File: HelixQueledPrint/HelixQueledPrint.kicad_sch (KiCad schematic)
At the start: 48 parts, among them J1 USB_C_Receptacle_USB2.0_16P, J101 Conn_Coaxial, SW1 SW_SPST, SW2 SW_SPST, U101 ESP32-C6FHx, U102 BGS12WN6E6327, Y1 40MHz

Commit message: added some stuffs
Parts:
- added R17: 0R, Resistor_SMD:R_0402_1005Metric, symbol Device:R
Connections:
- net at R101.1, R102.2, U102.6 (CTRL): now also R17.1
- net GPIO15: now reaches U101.19 (GPIO15)
- net GPIO15: now also R17.2
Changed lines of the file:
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@@
 	)
 	(junction
-		(at 25.4 96.52)
-		(diameter 0)
-		(color 0 0 0 0)
-	)
-	(junction
 		(at 184.15 217.17)
 		(diameter 0)
@@
 	)
 	(junction
+		(at 116.84 121.92)
+		(diameter 0)
+		(color 0 0 0 0)
+	)
+	(junction
 		(at 203.2 163.83)
 		(diameter 0)
@@
 	(wire
 		(pts
-			(xy 21.59 96.52) (xy 25.4 96.52)
+			(xy 391.16 43.18) (xy 335.28 43.18)
 		)
 		(stroke
@@
 	(wire
 		(pts
-			(xy 391.16 43.18) (xy 335.28 43.18)
+			(xy 193.04 27.94) (xy 193.04 33.02)
 		)
 		(stroke
@@
 	(wire
 		(pts
-			(xy 193.04 27.94) (xy 193.04 33.02)
+			(xy 248.92 109.22) (xy 246.38 109.22)
 		)
 		(stroke
@@
 	(wire
 		(pts
-			(xy 248.92 109.22) (xy 246.38 109.22)
+			(xy 375.92 21.59) (xy 391.16 21.59)
 		)
 		(stroke
@@
 	(wire
 		(pts
-			(xy 375.92 21.59) (xy 391.16 21.59)
+			(xy 383.54 113.03) (xy 383.54 33.02)
 		)
 		(stroke
@@
 	(wire
 		(pts
-			(xy 383.54 113.03) (xy 383.54 33.02)
+			(xy 116.84 130.81) (xy 116.84 133.35)
 		)
 		(stroke
@@
 	(wire
 		(pts
-			(xy 59.69 59.69) (xy 59.69 54.61)
-		)
-		(stroke
-			(width 0)
-			(type default)
-		)
-	)
-	(wire
-		(pts
 			(xy 386.08 88.9) (xy 386.08 29.21)
 		)
@@
 	(wire
 		(pts
-			(xy 44.45 54.61) (xy 48.26 54.61)
-		)
-		(stroke
-			(width 0)
-			(type default)
-		)
-	)
-	(wire
-		(pts
 			(xy 391.16 21.59) (xy 391.16 43.18)
 		)
@@
 	(wire
 		(pts
-			(xy 44.45 67.31) (xy 44.45 76.2)
-		)
-		(stroke
-			(width 0)
-			(type default)
-		)
-	)
-	(wire
-		(pts
 			(xy 200.66 129.54) (xy 200.66 134.62)
 		)
@@
 	(wire
 		(pts
-			(xy 55.88 54.61) (xy 59.69 54.61)
-		)
-		(stroke
-			(width 0)
-			(type default)
-		)
-	)
-	(wire
-		(pts
 			(xy 368.3 39.37) (xy 368.3 45.72)
 		)
@@
 	(wire
 		(pts
-			(xy 59.69 67.31) (xy 59.69 76.2)
-		)
-		(stroke
-			(width 0)
-			(type default)
-		)
-	)
-	(wire
-		(pts
 			(xy 335.28 88.9) (xy 386.08 88.9)
 		)
@@
 	(wire
 		(pts
-			(xy 44.45 54.61) (xy 44.45 59.69)
-		)
-		(stroke
-			(width 0)
-			(type default)
-		)
-	)
-	(wire
-		(pts
 			(xy 138.43 158.75) (xy 138.43 161.29)
 		)
@@
 	(wire
 		(pts
-			(xy 116.84 104.14) (xy 116.84 121.92)
-		)
-		(stroke
-			(width 0)
-			(type default)
-		)
-	)
-	(wire
-		(pts
 			(xy 128.27 171.45) (xy 128.27 168.91)
 		)
@@
 	(wire
 		(pts
+			(xy 116.84 104.14) (xy 116.84 121.92)
+		)
+		(stroke
+			(width 0)
+			(type default)
+		)
+	)
+	(wire
+		(pts
 			(xy 93.98 63.5) (xy 93.98 66.04)
 		)
@@
 	(wire
 		(pts
+			(xy 116.84 121.92) (xy 116.84 123.19)
+		)
+		(stroke
+			(width 0)
+			(type default)
+		)
+	)
+	(wire
+		(pts
 			(xy 139.7 44.45) (xy 139.7 49.53)
 		)
@@
 		)
 	)
+	(label "GPIO15"
+		(at 213.36 111.76 0)
+		(effects
+			(font
+				(size 1.27 1.27)
+			)
+			(justify left bottom)
+		)
+	)
 	(label "ENB"
 		(at 281.94 86.36 180)
@@
 		)
 	)
+	(label "GPIO15"
+		(at 116.84 133.35 270)
+		(effects
+			(font
+				(size 1.27 1.27)
+			)
+			(justify right bottom)
+		)
+	)
 	(label "GPIO8"
 		(at 195.58 129.54 270)
@@
 	)
 	(symbol
-		(lib_id "power:GND")
-		(at 44.45 76.2 0)
-		(unit 1)
-		(exclude_from_sim no)
-		(in_bom yes)
-		(on_board yes)
-		(dnp no)
-		(fields_autoplaced yes)
-		(property "Reference" "#PWR035"
-			(at 44.45 82.55 0)
-			(effects
-				(font
-					(size 1.27 1.27)
-				)
-				(hide yes)
-			)
-		)
-		(property "Value" "GND"
-			(at 44.45 81.28 0)
-			(effects
-				(font
-					(size 1.27 1.27)
-				)
-			)
-		)
-		(property "Footprint" ""
-			(at 44.45 76.2 0)
-			(effects
-				(font
-					(size 1.27 1.27)
-				)
-				(hide yes)
-			)
-		)
-		(property "Datasheet" ""
-			(at 44.45 76.2 0)
-			(effects
-				(font
-					(size 1.27 1.27)
-				)
-				(hide yes)
-			)
-		)
-		(property "Description" "Power symbol creates a global label with name \"GND\" , ground"
-			(at 44.45 76.2 0)
-			(effects
-				(font
-					(size 1.27 1.27)
-				)
-				(hide yes)
-			)
-		)
-		(pin "1"
-		)
-		(instances
-			(project "HelixQueledPrint"
-				(path "/398fd733-417c-46a8-b62a-83839861ebca"
-					(reference "#PWR035")
-					(unit 1)
-				)
-			)
-		)
-	)
-	(symbol
 		(lib_id "Device:C")
 		(at 193.04 36.83 0)
@@
 	)
 	(symbol
-		(lib_id "power:GND")
-		(at 59.69 76.2 0)
-		(unit 1)
-		(exclude_from_sim no)
-		(in_bom yes)
-		(on_board yes)
-		(dnp no)
-		(fields_autoplaced yes)
-		(property "Reference" "#PWR034"
-			(at 59.69 82.55 0)
-			(effects
-				(font
-					(size 1.27 1.27)
-				)
-				(hide yes)
-			)
-		)
-		(property "Value" "GND"
-			(at 59.69 81.28 0)
-			(effects
-				(font
-					(size 1.27 1.27)
-				)
-			)
-		)
-		(property "Footprint" ""
-			(at 59.69 76.2 0)
-			(effects
-				(font
-					(size 1.27 1.27)
-				)
-				(hide yes)
-			)
-		)
-		(property "Datasheet" ""
-			(at 59.69 76.2 0)
-			(effects
-				(font
-					(size 1.27 1.27)
-				)
-				(hide yes)
-			)
-		)
-		(property "Description" "Power symbol creates a global label with name \"GND\" , ground"
-			(at 59.69 76.2 0)
-			(effects
-				(font
-					(size 1.27 1.27)
-				)
-				(hide yes)
-			)
-		)
-		(pin "1"
-		)
-		(instances
-			(project "HelixQueledPrint"
-				(path "/398fd733-417c-46a8-b62a-83839861ebca"
-					(reference "#PWR034")
-					(unit 1)
-				)
-			)
-		)
-	)
-	(symbol
 		(lib_id "power:+3V3")
 		(at 152.4 21.59 0)
@@
 					(unit 1)
 				)
+			)
+		)
+	)
+	(symbol
+		(lib_id "Device:R")
+		(at 116.84 127 0)
+		(unit 1)
+		(exclude_from_sim no)
+		(in_bom yes)
+		(on_board yes)
+		(dnp yes)
+		(fields_autoplaced yes)
+		(property "Reference" "R17"
+			(at 119.38 125.7299 0)
+			(effects
+				(font
+					(size 1.27 1.27)
+				)
+				(justify left)
+			)
+		)
+		(property "Value" "0R"
+			(at 119.38 128.2699 0)
+			(effects
+				(font
+					(size 1.27 1.27)
+				)
+				(justify left)
+			)
+		)
+		(property "Footprint" "Resistor_SMD:R_0402_1005Metric"
+			(at 115.062 127 90)
+			(effects
+				(font
+					(size 1.27 1.27)
+				)
+				(hide yes)
+			)
+		)
+		(property "Datasheet" "~"
+			(at 116.84 127 0)
+			(effects
+				(font
+					(size 1.27 1.27)
+				)
+				(hide yes)
+			)
+		)
+		(property "Description" "Resistor"
+			(at 116.84 127 0)
+			(effects
+				(font
+					(size 1.27 1.27)
+				)
+				(hide yes)
+			)
+		)
+		(pin "2"
+		)
+		(pin "1"
+		)
+		(instances
+			(project "HelixQueledPrint"
+				(path "/398fd733-417c-46a8-b62a-83839861ebca"
+					(reference "R17")
+					(unit 1)
+				)

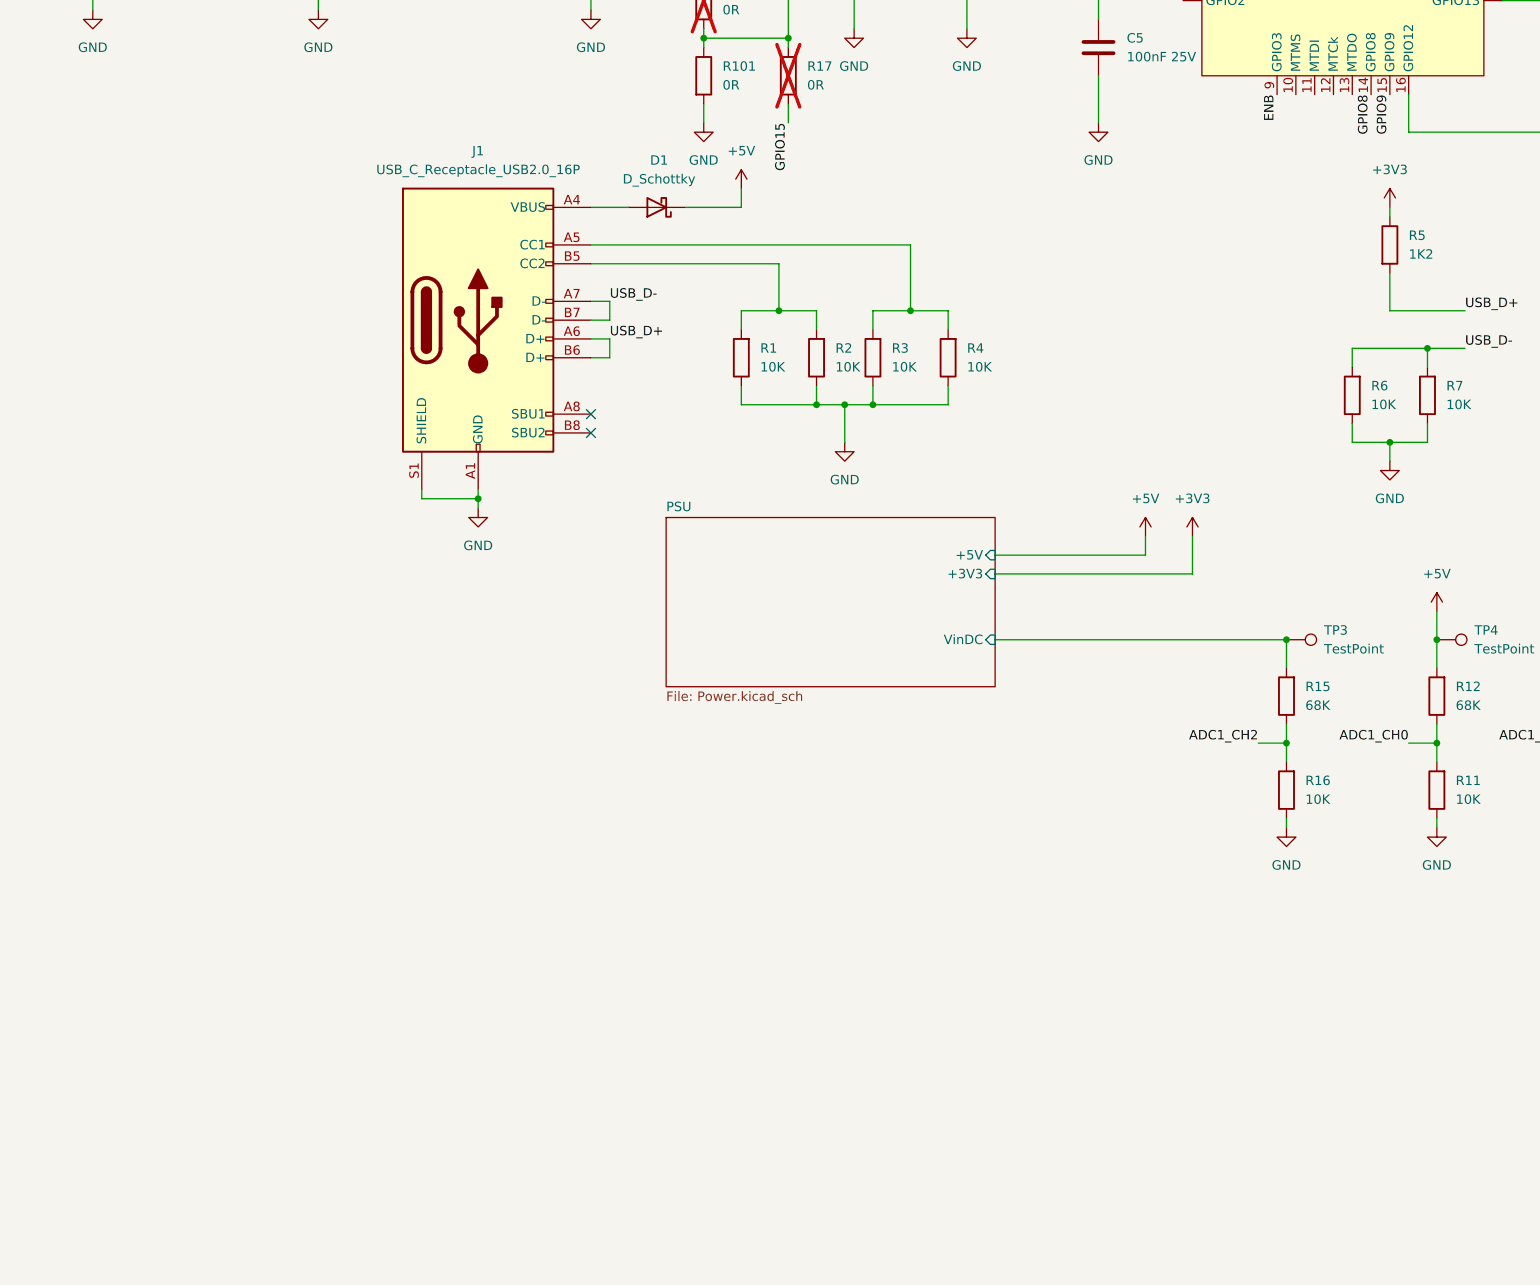
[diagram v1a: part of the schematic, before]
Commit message: added usb-pd trigger
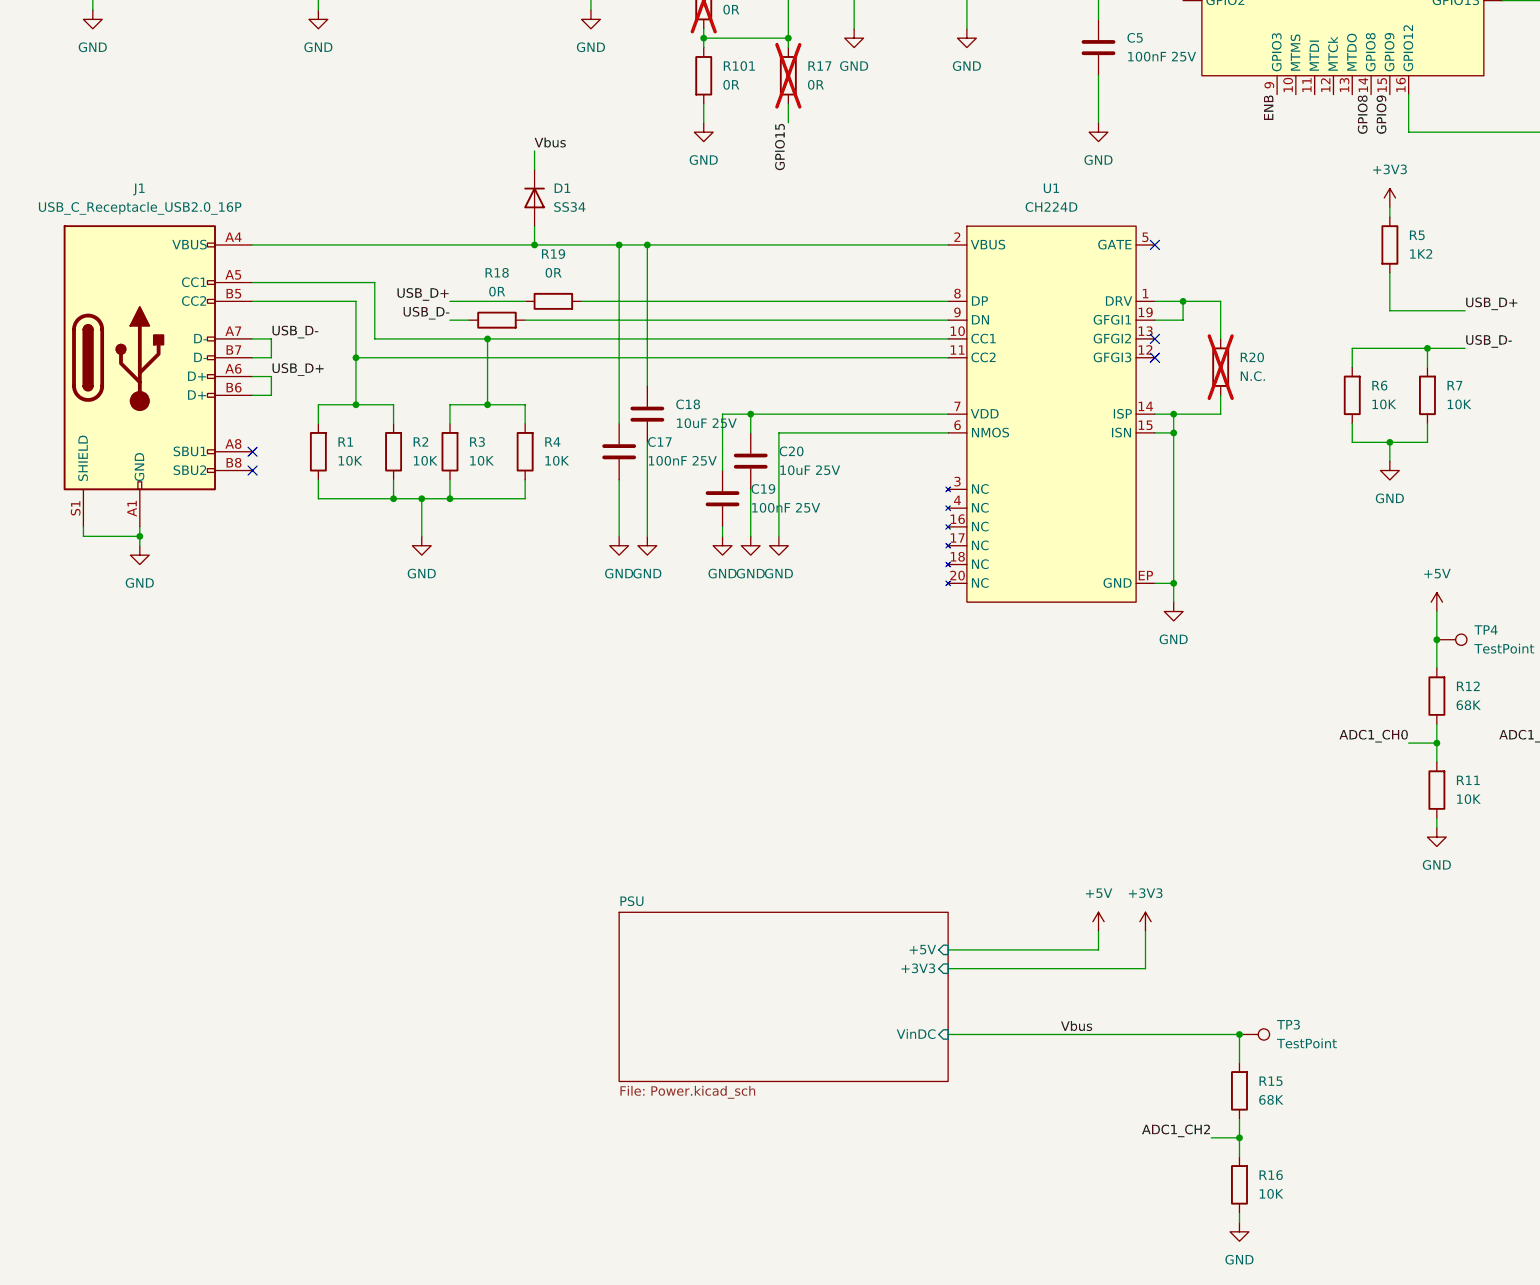
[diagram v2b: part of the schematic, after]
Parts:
- removed D1: D_Schottky, Diode_SMD:D_SOD-110, symbol Device:D_Schottky
- added C17, C19: 100nF 25V, Capacitor_SMD:C_0402_1005Metric, symbol Device:C
- added C18, C20: 10uF 25V, Capacitor_SMD:C_0805_2012Metric, symbol Device:C
- added D1: SS34, VE_diodes:SMA, symbol Device:D
- added R18, R19: 0R, Resistor_SMD:R_0402_1005Metric, symbol Device:R
- added R20: N.C., Resistor_SMD:R_0402_1005Metric, symbol Device:R
- added U1: CH224D, Package_DFN_QFN:QFN-20-1EP_3x3mm_P0.4mm_EP1.65x1.65mm_ThermalVias, symbol 1CustomFootprints:CH224D
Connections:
- net GND: now also C17.2, C18.2, C19.2, C20.2, R20.2, U1.14 (ISP), U1.15 (ISN), U1.6 (NMOS), U1.EP (GND)
- net USB_D+: now also R19.1
- net USB_D-: now also R18.1
- net at J1.B5 (CC2), R1.2, R2.2: now also U1.11 (CC2)
- net at J1.A5 (CC1), R3.2, R4.2: now also U1.10 (CC1)
- net at J1.A4 (VBUS), J1.A9 (VBUS), J1.B4 (VBUS)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: now also C17.1, C18.1, D1.2 (A), U1.2 (VBUS)
- net PSU/VinDC renamed Vbus
- net Vbus: now also D1.1 (K)
- new net: R20.1, U1.1 (DRV), U1.19 (GFGI1)
- new net: C19.1, C20.1, U1.7 (VDD)
- new net: R19.2, U1.8 (DP)
- new net: R18.2, U1.9 (DN)
- no-connect marks 2 -> 5
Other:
- moved on the sheet: J1, R1, R15, R16, R2, R3, R4, TP3

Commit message: finished (i think)
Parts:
- removed R101, R102, R17: 0R, Resistor_SMD:R_0402_1005Metric, symbol Device:R
- removed U102: BGS12WN6E6327, Package_LGA:Infineon_PG-TSNP-6-10_0.7x1.1mm_0.7x1.1mm_P0.4mm, symbol RF_Switch:BGS12WN6E6327
- added C101, C102, C103: C, Capacitor_SMD:C_0402_1005Metric, symbol Device:C
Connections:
- net GND: now also U1.21 (GND); no longer U1.EP (GND)
- net at AE101.1 (A): now also C101.1, C102.1
- net at J101.1 (In): now also C101.2, C103.1
- net at C13.1, L1.1: now also C102.2, C103.2
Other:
- moved on the sheet: AE101, J101, R15, R16, TP3
